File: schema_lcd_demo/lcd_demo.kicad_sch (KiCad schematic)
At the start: 7 parts, among them U1 Pico, U2 LCD20x4_HD44780, U3 LCD20x4_HD44780, U4 LCD20x4_HD44780

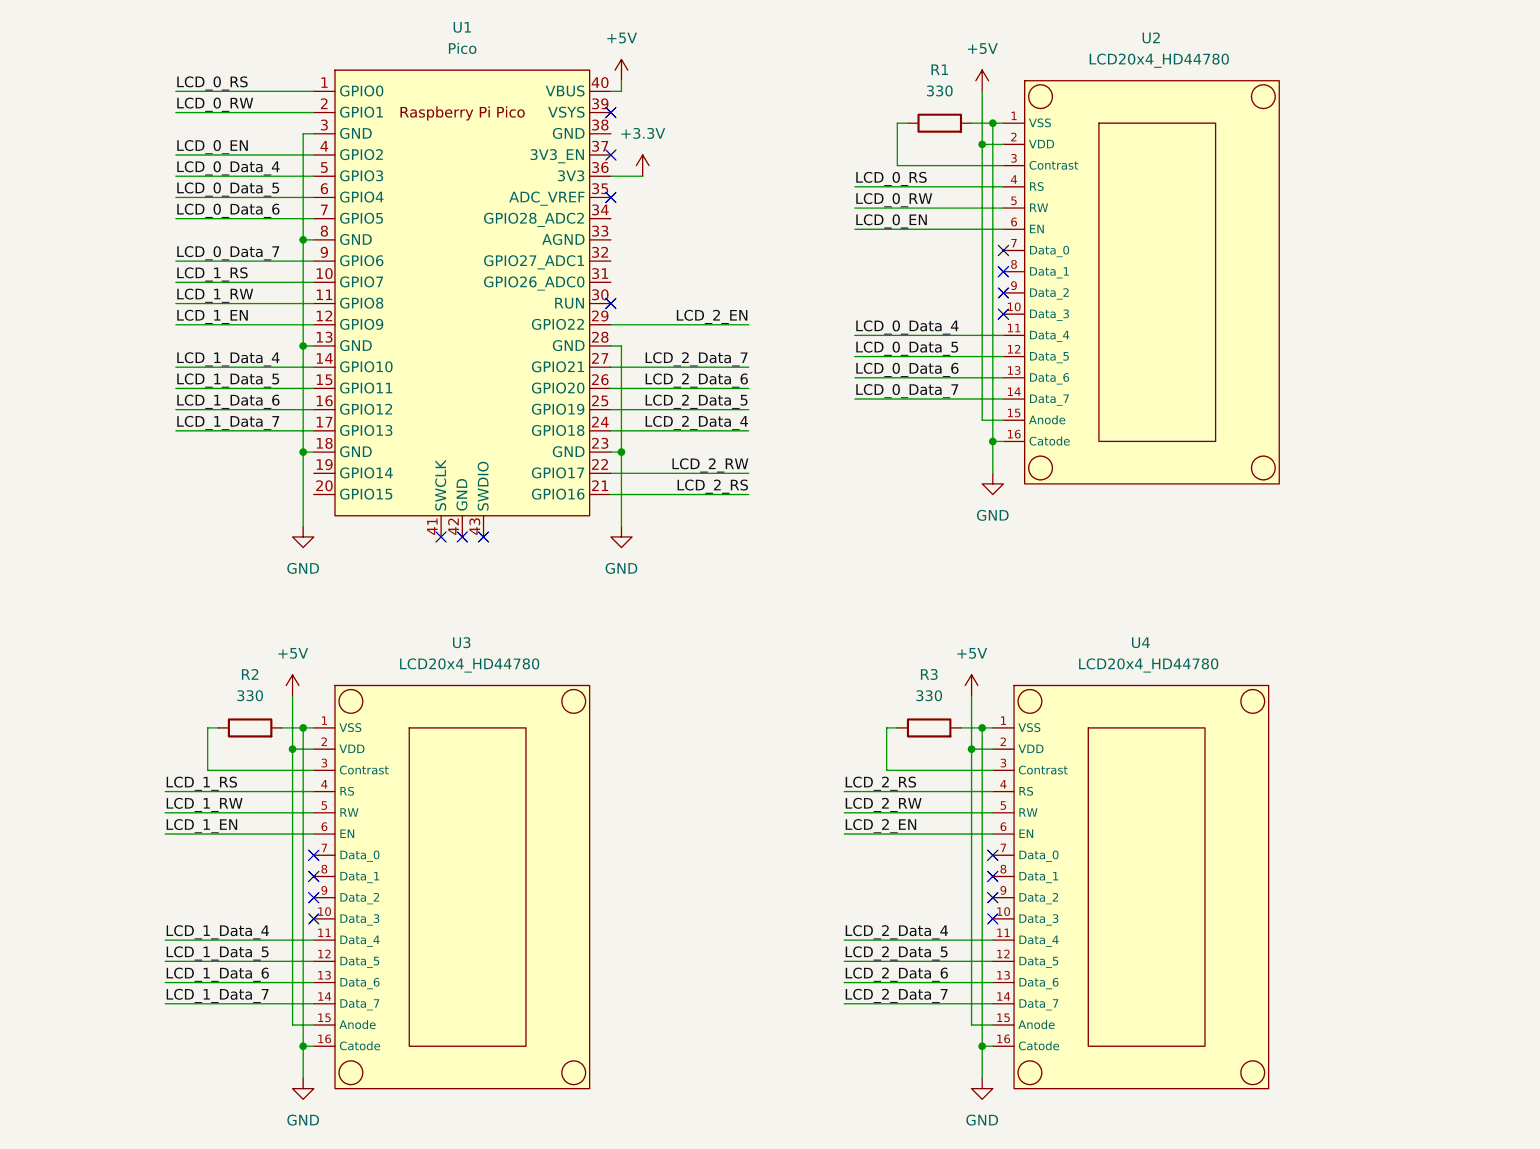
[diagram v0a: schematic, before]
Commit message: Deleted third lcd from schema
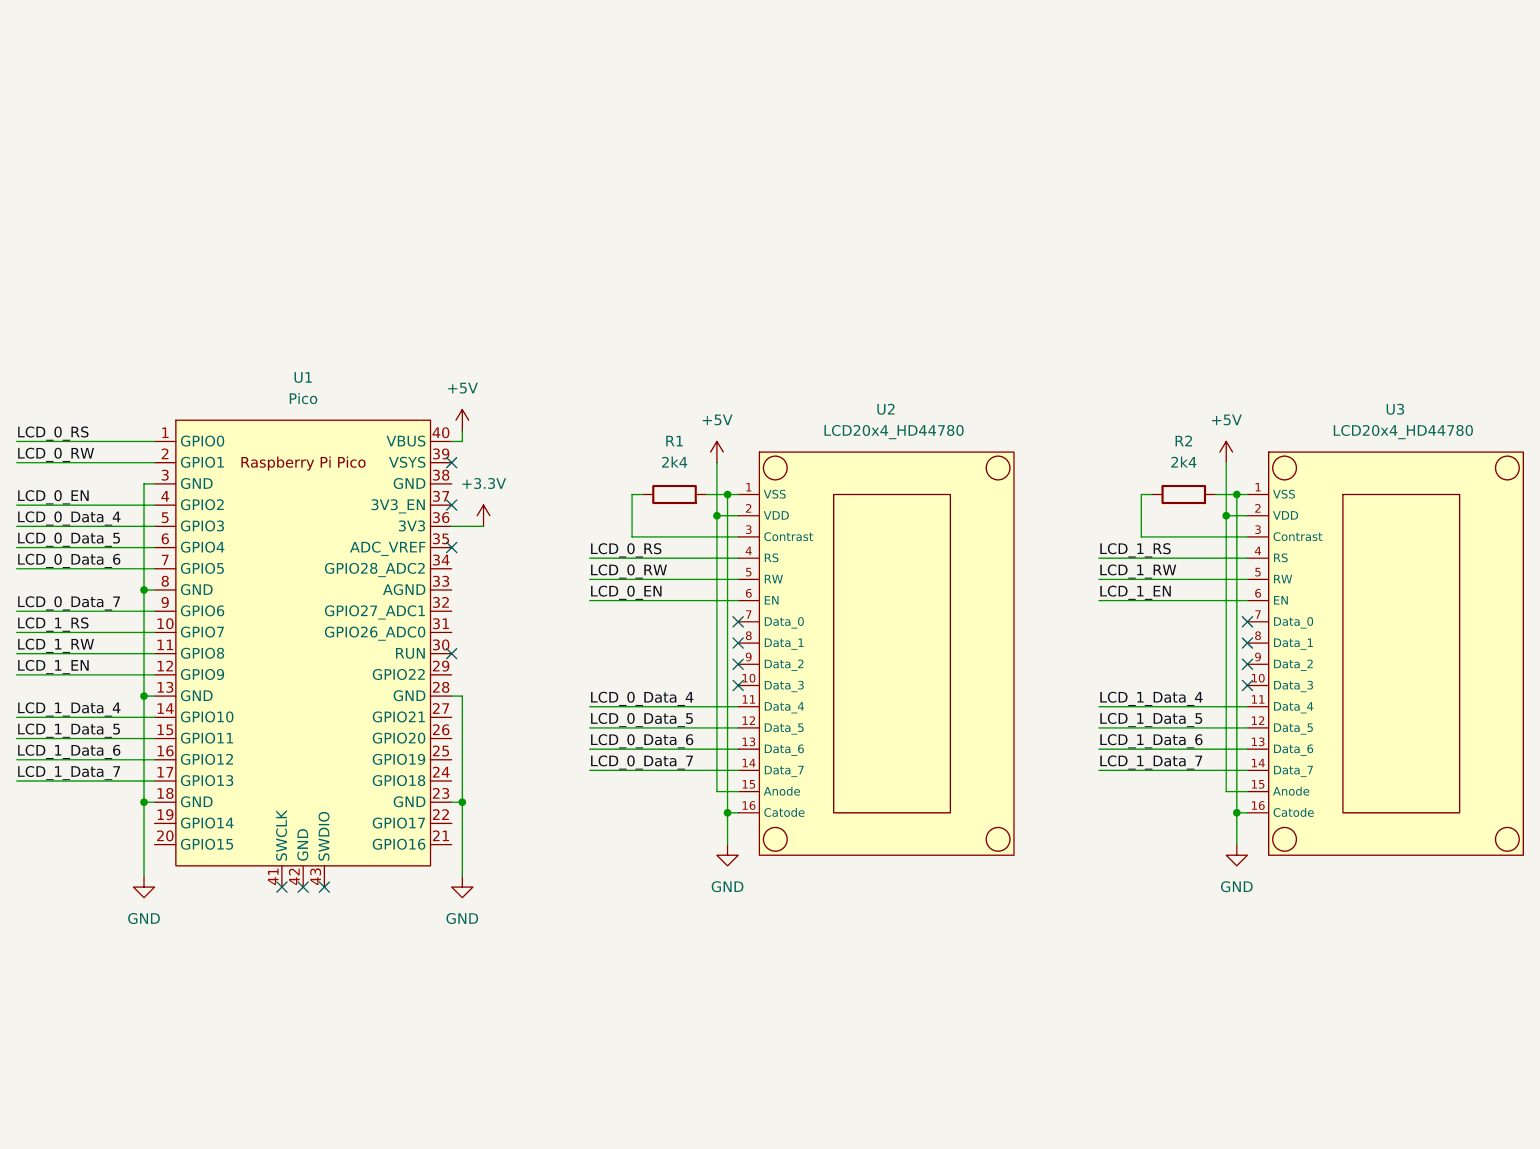
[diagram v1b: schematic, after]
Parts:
- removed R3: 330, Resistor_SMD:R_2010_5025Metric, symbol Device:R
- removed U4: LCD20x4_HD44780, HD44780:HD44780 2004A, symbol HD44780:LCD20x4_HD44780
- R1, R2: value 330 -> 2k4
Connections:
- net LCD_2_Data_4: no longer names the net of U1.24 (GPIO18)
- net LCD_2_Data_5: no longer names the net of U1.25 (GPIO19)
- net LCD_2_Data_6: no longer names the net of U1.26 (GPIO20)
- net LCD_2_Data_7: no longer names the net of U1.27 (GPIO21)
- net LCD_2_EN: no longer names the net of U1.29 (GPIO22)
- net LCD_2_RS: no longer names the net of U1.21 (GPIO16)
- net LCD_2_RW: no longer names the net of U1.22 (GPIO17)
- no-connect marks 19 -> 15
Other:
- moved on the sheet: R1, R2, U1, U2, U3
